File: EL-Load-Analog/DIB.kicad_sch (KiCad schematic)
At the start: 7 parts, among them J3 Conn_02x06_Odd_Even, U5 24LC32, X3 DIB Pheriperal connector

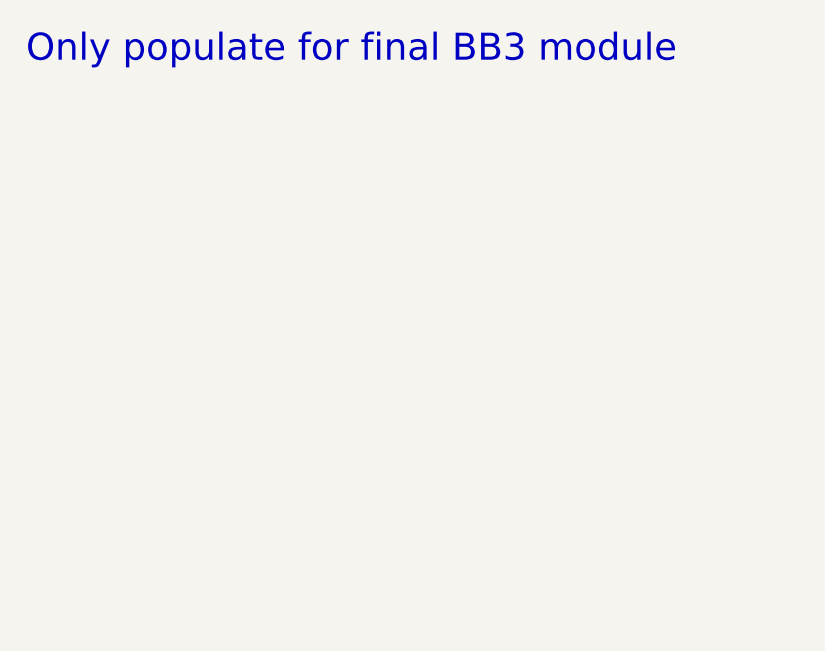
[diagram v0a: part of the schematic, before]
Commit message: Added heatsink moutingholes, reverse polarity, moved snubbers.
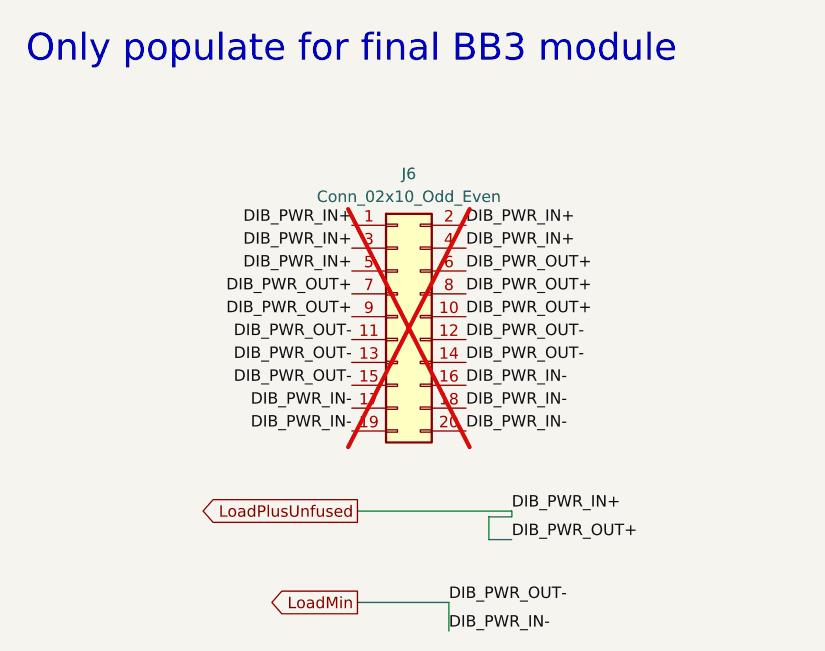
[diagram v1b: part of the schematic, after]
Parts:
- added J6: Conn_02x10_Odd_Even, Connector_PinSocket_2.54mm:PinSocket_2x10_P2.54mm_Horizontal, symbol Connector_Generic:Conn_02x10_Odd_Even
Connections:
- new net LoadMin: J6.11 (Pin_11), J6.12 (Pin_12), J6.13 (Pin_13), J6.14 (Pin_14), J6.15 (Pin_15), J6.16 (Pin_16), J6.17 (Pin_17), J6.18 (Pin_18), J6.19 (Pin_19), J6.20 (Pin_20)
- new net LoadPlusUnfused: J6.1 (Pin_1), J6.10 (Pin_10), J6.2 (Pin_2), J6.3 (Pin_3), J6.4 (Pin_4), J6.5 (Pin_5), J6.6 (Pin_6), J6.7 (Pin_7), J6.8 (Pin_8), J6.9 (Pin_9)
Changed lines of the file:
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@@
+    (stroke (width 0) (type default))
+  )
+  (wire (pts (xy 182.245 138.43) (xy 179.705 138.43))
+    (stroke (width 0) (type default))
+  )
+  (wire (pts (xy 165.1 147.955) (xy 175.26 147.955))
     (stroke (width 0) (type default))
   )
@@
     (stroke (width 0) (type default))
   )
+  (wire (pts (xy 179.705 138.43) (xy 179.705 140.97))
+    (stroke (width 0) (type default))
+  )
   (wire (pts (xy 32.385 44.45) (xy 32.385 62.23))
     (stroke (width 0) (type default))
   )
+  (wire (pts (xy 179.705 140.97) (xy 182.245 140.97))
+    (stroke (width 0) (type default))
+  )
   (wire (pts (xy 89.535 49.53) (xy 89.535 54.61))
     (stroke (width 0) (type default))
@@
     (stroke (width 0) (type default))
   )
+  (wire (pts (xy 175.26 147.955) (xy 175.26 151.13))
+    (stroke (width 0) (type default))
+  )
   (wire (pts (xy 47.625 39.37) (xy 32.385 39.37))
     (stroke (width 0) (type default))
@@
     (stroke (width 0) (type default))
   )
+  (wire (pts (xy 182.245 137.795) (xy 182.245 138.43))
+    (stroke (width 0) (type default))
+  )
   (wire (pts (xy 60.96 111.125) (xy 77.47 111.125))
     (stroke (width 0) (type default))
@@
   )
   (wire (pts (xy 89.535 54.61) (xy 89.535 68.58))
+    (stroke (width 0) (type default))
+  )
+  (wire (pts (xy 165.1 137.795) (xy 182.245 137.795))
     (stroke (width 0) (type default))
   )
@@
     (effects (font (size 1.27 1.27)) (justify left bottom))
   )
+  (label "DIB_PWR_IN+" (at 164.465 111.125 180) (fields_autoplaced)
+    (effects (font (size 1.27 1.27)) (justify right bottom))
+  )
   (label "DIB_SCL" (at 178.435 40.64 0) (fields_autoplaced)
     (effects (font (size 1.27 1.27)) (justify left bottom))
   )
+  (label "DIB_PWR_OUT+" (at 164.465 113.665 180) (fields_autoplaced)
+    (effects (font (size 1.27 1.27)) (justify right bottom))
+  )
   (label "DIB_A1" (at 142.875 40.64 0) (fields_autoplaced)
     (effects (font (size 1.27 1.27)) (justify left bottom))
   )
+  (label "DIB_PWR_IN-" (at 164.465 126.365 180) (fields_autoplaced)
+    (effects (font (size 1.27 1.27)) (justify right bottom))
+  )
+  (label "DIB_PWR_OUT+" (at 177.165 113.665 0) (fields_autoplaced)
+    (effects (font (size 1.27 1.27)) (justify left bottom))
+  )
   (label "DIB_A2" (at 77.47 52.07 0) (fields_autoplaced)
     (effects (font (size 1.27 1.27)) (justify left bottom))
@@
     (effects (font (size 1.27 1.27)) (justify left bottom))
   )
+  (label "DIB_PWR_OUT+" (at 177.165 116.205 0) (fields_autoplaced)
+    (effects (font (size 1.27 1.27)) (justify left bottom))
+  )
   (label "DIB_CSB" (at 78.105 44.45 0) (fields_autoplaced)
     (effects (font (size 1.27 1.27)) (justify left bottom))
   )
+  (label "DIB_PWR_OUT+" (at 182.245 140.97 0) (fields_autoplaced)
+    (effects (font (size 1.27 1.27)) (justify left bottom))
+  )
+  (label "DIB_PWR_IN-" (at 177.165 123.825 0) (fields_autoplaced)
+    (effects (font (size 1.27 1.27)) (justify left bottom))
+  )
+  (label "DIB_PWR_OUT+" (at 177.165 111.125 0) (fields_autoplaced)
+    (effects (font (size 1.27 1.27)) (justify left bottom))
+  )
+  (label "DIB_PWR_IN+" (at 164.465 108.585 180) (fields_autoplaced)
+    (effects (font (size 1.27 1.27)) (justify right bottom))
+  )
+  (label "DIB_PWR_IN+" (at 182.245 137.795 0) (fields_autoplaced)
+    (effects (font (size 1.27 1.27)) (justify left bottom))
+  )
   (label "DIB_SDA" (at 178.435 38.1 0) (fields_autoplaced)
     (effects (font (size 1.27 1.27)) (justify left bottom))
   )
+  (label "DIB_PWR_OUT-" (at 164.465 121.285 180) (fields_autoplaced)
+    (effects (font (size 1.27 1.27)) (justify right bottom))
+  )
   (label "DIB_SCL" (at 38.735 36.83 0) (fields_autoplaced)
     (effects (font (size 1.27 1.27)) (justify left bottom))
@@
     (effects (font (size 1.27 1.27)) (justify left bottom))
   )
+  (label "DIB_PWR_IN+" (at 164.465 106.045 180) (fields_autoplaced)
+    (effects (font (size 1.27 1.27)) (justify right bottom))
+  )
+  (label "DIB_PWR_IN+" (at 177.165 106.045 0) (fields_autoplaced)
+    (effects (font (size 1.27 1.27)) (justify left bottom))
+  )
+  (label "DIB_PWR_OUT-" (at 175.26 147.955 0) (fields_autoplaced)
+    (effects (font (size 1.27 1.27)) (justify left bottom))
+  )
+  (label "DIB_PWR_OUT-" (at 177.165 121.285 0) (fields_autoplaced)
+    (effects (font (size 1.27 1.27)) (justify left bottom))
+  )
   (label "DIB_A0" (at 142.875 38.1 0) (fields_autoplaced)
     (effects (font (size 1.27 1.27)) (justify left bottom))
   )
+  (label "DIB_PWR_OUT+" (at 164.465 116.205 180) (fields_autoplaced)
+    (effects (font (size 1.27 1.27)) (justify right bottom))
+  )
   (label "DIB_MOSI" (at 37.465 49.53 0) (fields_autoplaced)
     (effects (font (size 1.27 1.27)) (justify left bottom))
   )
+  (label "DIB_PWR_OUT-" (at 177.165 118.745 0) (fields_autoplaced)
+    (effects (font (size 1.27 1.27)) (justify left bottom))
+  )
   (label "DIB_~{RESET}" (at 78.105 34.29 0) (fields_autoplaced)
     (effects (font (size 1.27 1.27)) (justify left bottom))
@@
     (effects (font (size 1.27 1.27)) (justify left bottom))
   )
+  (label "DIB_PWR_IN-" (at 164.465 128.905 180) (fields_autoplaced)
+    (effects (font (size 1.27 1.27)) (justify right bottom))
+  )
+  (label "DIB_PWR_IN-" (at 177.165 126.365 0) (fields_autoplaced)
+    (effects (font (size 1.27 1.27)) (justify left bottom))
+  )
+  (label "DIB_PWR_OUT-" (at 164.465 118.745 180) (fields_autoplaced)
+    (effects (font (size 1.27 1.27)) (justify right bottom))
+  )
+  (label "DIB_PWR_IN-" (at 175.26 151.13 0) (fields_autoplaced)
+    (effects (font (size 1.27 1.27)) (justify left bottom))
+  )
   (label "DIB_CSA" (at 37.465 41.91 0) (fields_autoplaced)
     (effects (font (size 1.27 1.27)) (justify left bottom))
@@
     (effects (font (size 1.27 1.27)) (justify left bottom))
   )
+  (label "DIB_PWR_OUT-" (at 164.465 123.825 180) (fields_autoplaced)
+    (effects (font (size 1.27 1.27)) (justify right bottom))
+  )
   (label "DIB_A0" (at 37.465 52.07 0) (fields_autoplaced)
     (effects (font (size 1.27 1.27)) (justify left bottom))
@@
     (effects (font (size 1.27 1.27)) (justify left bottom))
   )
+  (label "DIB_PWR_IN-" (at 177.165 128.905 0) (fields_autoplaced)
+    (effects (font (size 1.27 1.27)) (justify left bottom))
+  )
+  (label "DIB_PWR_IN+" (at 177.165 108.585 0) (fields_autoplaced)
+    (effects (font (size 1.27 1.27)) (justify left bottom))
+  )
   (label "DIB_MISO" (at 78.105 46.99 0) (fields_autoplaced)
     (effects (font (size 1.27 1.27)) (justify left bottom))
+  )
+  (global_label "LoadMin" (shape output) (at 165.1 147.955 180) (fields_autoplaced)
+    (effects (font (size 1.27 1.27)) (justify right))
+    (property "Intersheetrefs" "${INTERSHEET_REFS}" (at 155.0064 147.8756 0)
+      (effects (font (size 1.27 1.27)) (justify right))
+    )
+  )
+  (global_label "LoadPlusUnfused" (shape output) (at 165.1 137.795 180) (fields_autoplaced)
+    (effects (font (size 1.27 1.27)) (justify right))
+    (property "Intersheetrefs" "${INTERSHEET_REFS}" (at 145.9075 137.795 0)
+      (effects (font (size 1.27 1.27)) (justify right))
+    )
   )
   (symbol (lib_id "EEZ-DIB:GND-DIB") (at 32.385 67.945 0) (unit 1)
@@
         )
       )
+    )
+  )
+  (symbol (lib_id "Connector_Generic:Conn_02x10_Odd_Even") (at 169.545 116.205 0) (unit 1)
+    (in_bom no) (on_board no) (dnp yes) (fields_autoplaced)
+    (property "Reference" "J6" (at 170.815 100.33 0)
+      (effects (font (size 1.27 1.27)))
+    )
+    (property "Value" "Conn_02x10_Odd_Even" (at 170.815 102.87 0)
+      (effects (font (size 1.27 1.27)))
+    )
+    (property "Footprint" "Connector_PinSocket_2.54mm:PinSocket_2x10_P2.54mm_Horizontal" (at 169.545 116.205 0)
+      (effects (font (size 1.27 1.27)) hide)
+    )
+    (property "Datasheet" "~" (at 169.545 116.205 0)
+      (effects (font (size 1.27 1.27)) hide)
+    )
+    (pin "4")
+    (pin "16")
+    (pin "1")
+    (pin "9")
+    (pin "17")
+    (pin "5")
+    (pin "20")
+    (pin "12")
+    (pin "8")
+    (pin "13")
+    (pin "3")
+    (pin "7")
+    (pin "10")
+    (pin "11")
+    (pin "18")
+    (pin "19")
+    (pin "2")
+    (pin "6")
+    (pin "15")
+    (pin "14")
+    (instances
+      (project "EL-Load-Analog"
+        (path "/51d9228f-95b8-4f0d-bdba-83c3975c517c/11723597-8dfc-4b1a-a2ae-7a0fb5ce6508"
+          (reference "J6") (unit 1)
+        )
+      )

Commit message: v4 Analog board design. Features reverse polarity, remote sense error and new clamping circuitry.
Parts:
- C13: Part Name C_100.0nF_0805_20% -> C_100.0nF_50V_0805_10%_X7R
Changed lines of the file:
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@@
   (title_block
     (title "Electronic Load Analog Test Board")
-    (date "2024-02-06")
+    (date "2024-11-10")
     (rev "${VERSION}")
     (comment 1 "License: CERN-OHL-W-2.0")
@@
       (effects (font (size 1.27 1.27)) hide)
     )
-    (property "Part Name" "C_100.0nF_0805_20%" (at 173.99 29.21 0)
-      (effects (font (size 1.27 1.27)) hide)
-    )
+    (property "Part Name" "C_100.0nF_50V_0805_10%_X7R " (at 173.99 29.21 0)
+      (effects (font (size 1.27 1.27)) hide)
+    )
